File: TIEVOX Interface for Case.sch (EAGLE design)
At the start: 23 parts, among them IC1 DMMT5401, Q1 DMP2305U-7, U4 CAT24C32.UDFN8

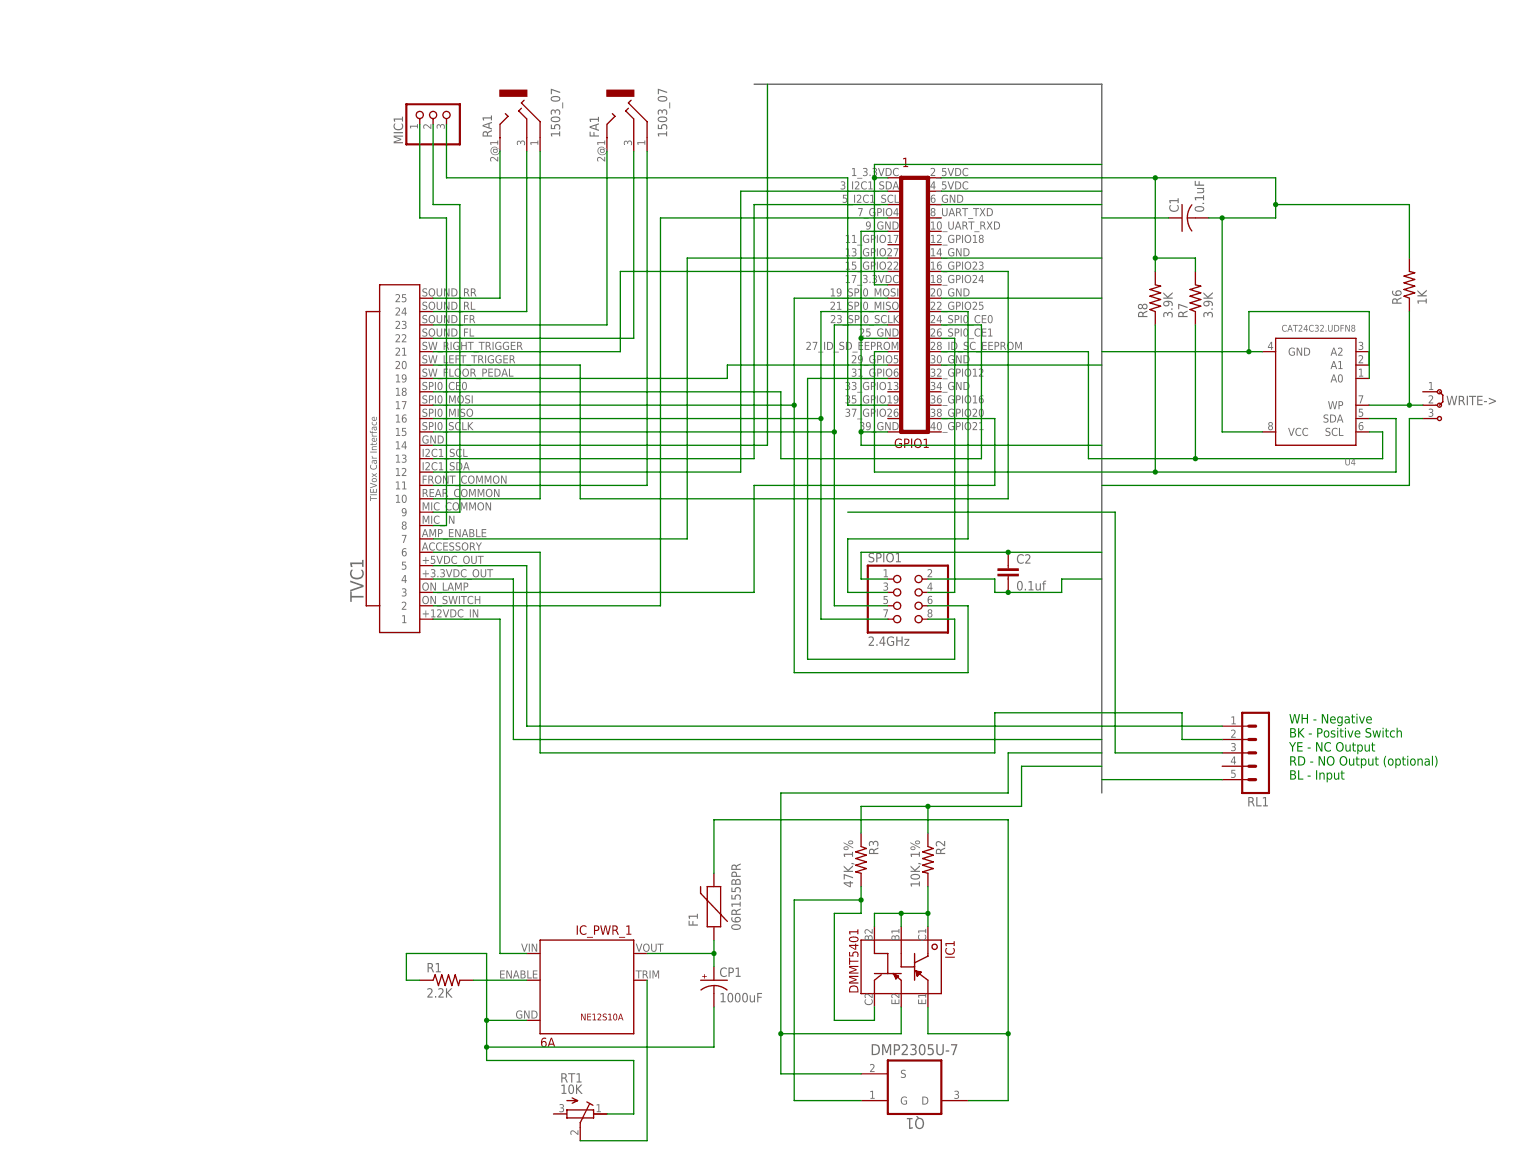
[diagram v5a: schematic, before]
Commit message: Should have working versions of all required boards now.
Updated to No Commercial license.
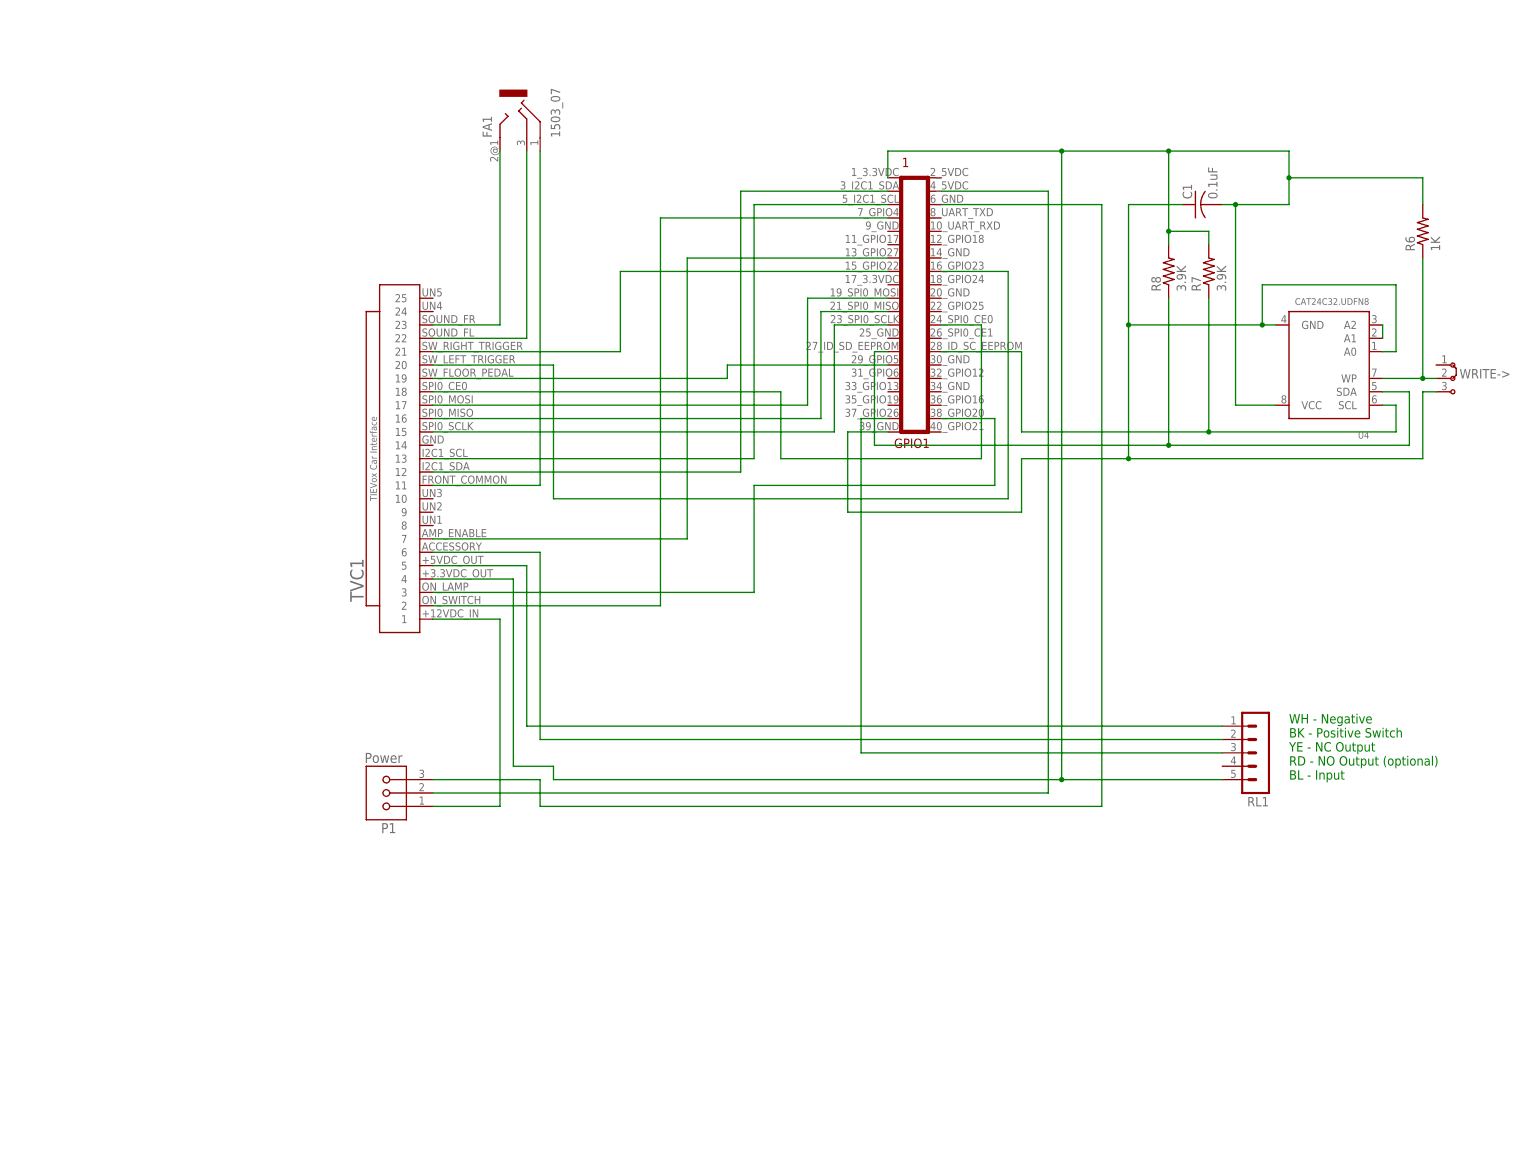
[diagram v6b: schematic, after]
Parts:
- removed C2: 0.1uf, capacitor-wima:C5/2.5
- removed CP1: 1000uF, rcl:CPOL-USE3.5-8
- removed F1: 06R155BPR, SparkFun-PowerIC:PTCPTH
- removed IC1: DMMT5401, Diodes_Inc_By_element14_Batch_1:DMMT5401DMMT
- removed IC_PWR_1: 6A, packages:NE12S12V6A
- removed MIC1: (no value), adafruit:PINHD-1X3
- removed Q1: DMP2305U-7, Diodes_Inc_By_element14_Batch_1:DMP2305U-7
- removed R1: 2.2K, adafruit:R-US_0207/10
- removed R2: 10K, 1%, adafruit:R-US_0207/7
- removed R3: 47K, 1%, adafruit:R-US_0207/7
- removed RA1: 1503_07, con-lumberg:1503_07
- removed RT1: 10K, resistor:R-TRIMM3006P
- removed SPIO1: 2.4GHz, pinhead:PINHD-2X4
- added P1: Power, connector:CONN3-L
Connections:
- removed net IN: F1.2, IC1.E1, Q1.D
- removed net N$11: GPIO1.31_GPIO6, SPIO1.8
- removed net N$12: RA1.2, TVC1.25
- removed net N$13: RA1.3, TVC1.24
- removed net N$16: MIC1.1, TVC1.8
- removed net N$17: MIC1.2, TVC1.9
- removed net N$22: GPIO1.35_GPIO19, MIC1.3
- removed net N$28: CP1.+, F1.1, IC_PWR_1.VOUT
- removed net N$29: IC_PWR_1.ENABLE, R1.2
- removed net N$32: IC1.B1, IC1.B2, IC1.C1, R2.2
- removed net N$33: IC1.C2, Q1.G, R3.2
- removed net N$4: GPIO1.22_GPIO25, SPIO1.3
- removed net N$6: RA1.1, TVC1.10
- removed net N$7: GPIO1.26_SPI0_CE1, SPIO1.4
- removed net PWR12_TRIM: IC_PWR_1.TRIM, RT1.S
- new net GND_39: C1.1, GPIO1.39_GND, U4.A0, U4.GND, WRITE->.3
- net +3.3VDC: no longer C2.2, GPIO1.17_3.3VDC, SPIO1.2
- net +5VDC: now also P1.2; no longer GPIO1.2_5VDC, IC1.E2, Q1.S
- net GND: now also P1.3; no longer C1.1, C2.1, CP1.-, GPIO1.14_GND, GPIO1.20_GND, GPIO1.25_GND, GPIO1.30_GND, GPIO1.39_GND, GPIO1.9_GND, IC_PWR_1.GND, R1.1, R2.1, R3.1, RT1.E, SPIO1.1, TVC1.14, U4.A0, U4.GND, WRITE->.3
- net N$10: no longer SPIO1.6
- net N$31: now also GPIO1.37_GPIO26
- net N$8: no longer SPIO1.5
- net N$9: no longer SPIO1.7
- net PWR12_IN: now also P1.1; no longer IC_PWR_1.VIN
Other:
- note removed: "SPI 2.4GHz nRF24L01P-MODULE-PCB"
- moved on the sheet: C1, FA1, R6, R7, R8, U4, WRITE->
